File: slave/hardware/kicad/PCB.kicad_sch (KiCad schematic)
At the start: 0 parts

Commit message: feat(HW): add System Power Source Sheet
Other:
- added sheet Source (source.kicad_sch)
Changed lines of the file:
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@@
 	(generator_version "10.0")
 	(paper "A4")
+	(sheet
+		(at 207.01 74.93)
+		(size 25.4 21.59)
+		(exclude_from_sim no)
+		(in_bom yes)
+		(on_board yes)
+		(dnp no)
+		(fields_autoplaced yes)
+		(stroke
+			(width 0.1524)
+			(type solid)
+		)
+		(fill
+			(color 0 0 0 0)
+		)
+		(property "Sheetname" "Source"
+			(at 207.01 74.2184 0)
+			(show_name no)
+			(do_not_autoplace no)
+			(effects
+				(font
+					(size 1.27 1.27)
+				)
+				(justify left bottom)
+			)
+		)
+		(property "Sheetfile" "source.kicad_sch"
+			(at 207.01 97.1046 0)
+			(show_name no)
+			(do_not_autoplace no)
+			(effects
+				(font
+					(size 1.27 1.27)
+				)
+				(justify left top)
+			)
+		)
+		(instances
+			(project "PCB"
+				(path "/53ac5407-c20a-483b-9c15-01b665bcfde4"
+					(page "2")
+				)
+			)
+		)
+	)
 	(sheet_instances
 		(path "/"

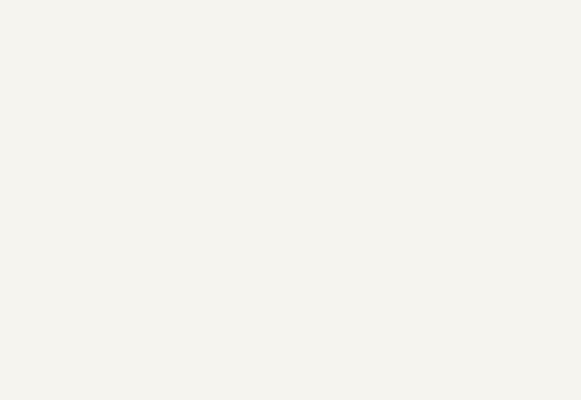
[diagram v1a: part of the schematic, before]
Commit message: feat(HW): start control sheet implementation
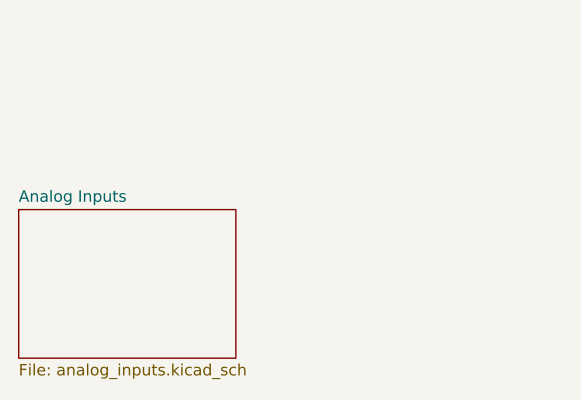
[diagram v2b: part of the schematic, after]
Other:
- added sheet Analog Inputs (analog_inputs.kicad_sch)
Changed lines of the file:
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@@
+		)
+	)
+	(sheet
+		(at 100.33 106.68)
+		(size 24.13 16.51)
+		(exclude_from_sim no)
+		(in_bom yes)
+		(on_board yes)
+		(dnp no)
+		(fields_autoplaced yes)
+		(stroke
+			(width 0.1524)
+			(type solid)
+		)
+		(fill
+			(color 0 0 0 0)
+		)
+		(property "Sheetname" "Analog Inputs"
+			(at 100.33 105.9684 0)
+			(show_name no)
+			(do_not_autoplace no)
+			(effects
+				(font
+					(size 1.27 1.27)
+				)
+				(justify left bottom)
+			)
+		)
+		(property "Sheetfile" "analog_inputs.kicad_sch"
+			(at 100.33 123.7746 0)
+			(show_name no)
+			(do_not_autoplace no)
+			(effects
+				(font
+					(size 1.27 1.27)
+				)
+				(justify left top)
+			)
+		)
+		(instances
+			(project "PCB"
+				(path "/53ac5407-c20a-483b-9c15-01b665bcfde4"
+					(page "3")
+				)
+			)
 		)
 	)

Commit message: feat(HW): add digital input circuit files
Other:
- added sheet Control (control.kicad_sch)
- added sheet Digital Inputs (digital_inputs.kicad_sch)
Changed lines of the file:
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@@
 	(paper "A4")
+	(sheet
+		(at 129.54 71.12)
+		(size 17.78 11.43)
+		(exclude_from_sim no)
+		(in_bom yes)
+		(on_board yes)
+		(dnp no)
+		(fields_autoplaced yes)
+		(stroke
+			(width 0.1524)
+			(type solid)
+		)
+		(fill
+			(color 0 0 0 0)
+		)
+		(property "Sheetname" "Control"
+			(at 129.54 70.4084 0)
+			(show_name no)
+			(do_not_autoplace no)
+			(effects
+				(font
+					(size 1.27 1.27)
+				)
+				(justify left bottom)
+			)
+		)
+		(property "Sheetfile" "control.kicad_sch"
+			(at 129.54 83.1346 0)
+			(show_name no)
+			(do_not_autoplace no)
+			(effects
+				(font
+					(size 1.27 1.27)
+				)
+				(justify left top)
+			)
+		)
+		(instances
+			(project "PCB"
+				(path "/53ac5407-c20a-483b-9c15-01b665bcfde4"
+					(page "4")
+				)
+			)
+		)
+	)
+	(sheet
+		(at 54.61 62.23)
+		(size 19.05 15.24)
+		(exclude_from_sim no)
+		(in_bom yes)
+		(on_board yes)
+		(dnp no)
+		(fields_autoplaced yes)
+		(stroke
+			(width 0.1524)
+			(type solid)
+		)
+		(fill
+			(color 0 0 0 0)
+		)
+		(property "Sheetname" "Digital Inputs"
+			(at 54.61 61.5184 0)
+			(show_name no)
+			(do_not_autoplace no)
+			(effects
+				(font
+					(size 1.27 1.27)
+				)
+				(justify left bottom)
+			)
+		)
+		(property "Sheetfile" "digital_inputs.kicad_sch"
+			(at 54.61 78.0546 0)
+			(show_name no)
+			(do_not_autoplace no)
+			(effects
+				(font
+					(size 1.27 1.27)
+				)
+				(justify left top)
+			)
+		)
+		(instances
+			(project "PCB"
+				(path "/53ac5407-c20a-483b-9c15-01b665bcfde4"
+					(page "5")
+				)
+			)
+		)
+	)
 	(sheet
 		(at 207.01 74.93)

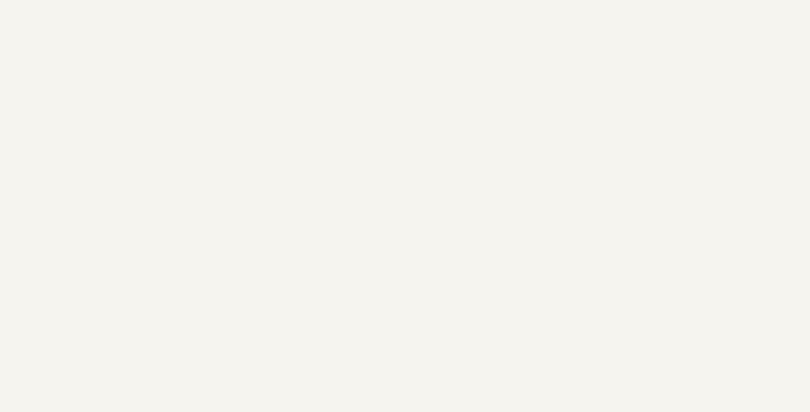
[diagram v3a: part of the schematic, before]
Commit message: feat(HW): create communication schematic with CAN and I2C level shifter
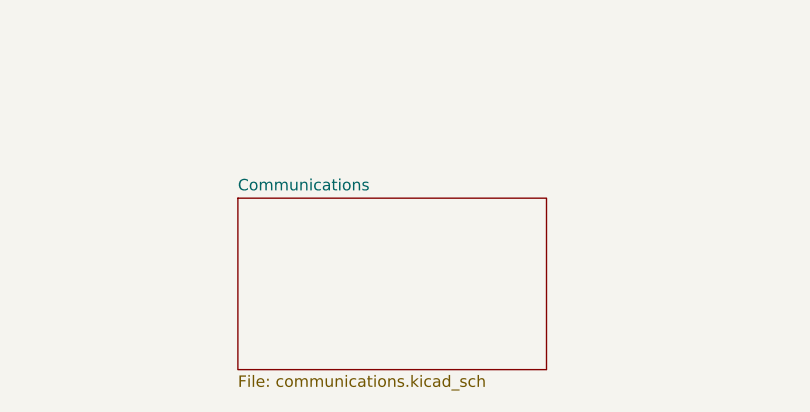
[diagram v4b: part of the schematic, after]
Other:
- added sheet Communications (communications.kicad_sch)
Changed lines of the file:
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@@
+		)
+	)
+	(sheet
+		(at 160.02 128.27)
+		(size 34.29 19.05)
+		(exclude_from_sim no)
+		(in_bom yes)
+		(on_board yes)
+		(dnp no)
+		(fields_autoplaced yes)
+		(stroke
+			(width 0.1524)
+			(type solid)
+		)
+		(fill
+			(color 0 0 0 0)
+		)
+		(property "Sheetname" "Communications"
+			(at 160.02 127.5584 0)
+			(show_name no)
+			(do_not_autoplace no)
+			(effects
+				(font
+					(size 1.27 1.27)
+				)
+				(justify left bottom)
+			)
+		)
+		(property "Sheetfile" "communications.kicad_sch"
+			(at 160.02 147.9046 0)
+			(show_name no)
+			(do_not_autoplace no)
+			(effects
+				(font
+					(size 1.27 1.27)
+				)
+				(justify left top)
+			)
+		)
+		(instances
+			(project "PCB"
+				(path "/53ac5407-c20a-483b-9c15-01b665bcfde4"
+					(page "6")
+				)
+			)
 		)
 	)

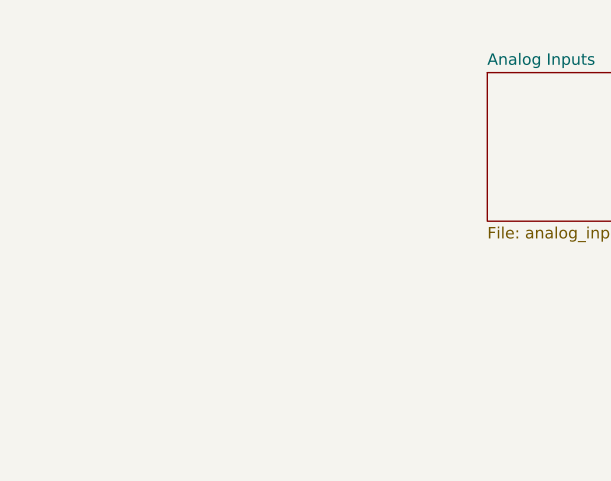
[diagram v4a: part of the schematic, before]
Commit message: feat(HW): add initial schematic pages
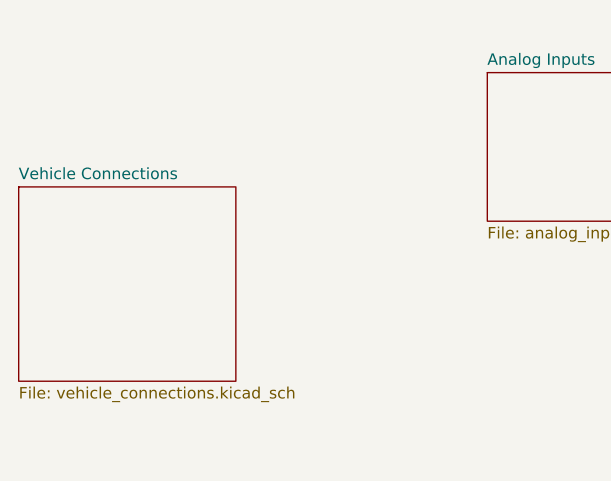
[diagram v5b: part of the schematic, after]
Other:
- added sheet Vehicle Connections (vehicle_connections.kicad_sch)
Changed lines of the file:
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@@
+	)
+	(sheet
+		(at 48.26 119.38)
+		(size 24.13 21.59)
+		(exclude_from_sim no)
+		(in_bom yes)
+		(on_board yes)
+		(dnp no)
+		(fields_autoplaced yes)
+		(stroke
+			(width 0.1524)
+			(type solid)
+		)
+		(fill
+			(color 0 0 0 0)
+		)
+		(property "Sheetname" "Vehicle Connections"
+			(at 48.26 118.6684 0)
+			(show_name no)
+			(do_not_autoplace no)
+			(effects
+				(font
+					(size 1.27 1.27)
+				)
+				(justify left bottom)
+			)
+		)
+		(property "Sheetfile" "vehicle_connections.kicad_sch"
+			(at 48.26 141.5546 0)
+			(show_name no)
+			(do_not_autoplace no)
+			(effects
+				(font
+					(size 1.27 1.27)
+				)
+				(justify left top)
+			)
+		)
+		(instances
+			(project "PCB"
+				(path "/53ac5407-c20a-483b-9c15-01b665bcfde4"
+					(page "7")
+				)
+			)
+		)
 	)
 	(sheet
